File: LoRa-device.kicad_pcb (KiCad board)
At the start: 2 copper layers, 86.4 x 50.8 mm, 102 parts, among them J1 USB_C_Receptacle_USB2.0_14P, J2 Conn_01x02_Pin, J3 Conn_Coaxial, J4 Conn_01x14_Pin, J5 U.FL, J6 Conn_01x04_Pin, J7 Conn_01x11_Pin, Q1 AO3401A, Q2 S8050, Q3 AO3401A, SW1 SW_Nidec_CAS-120A1, U1 ESP32-S3, U2 W25Q128JVS, U3 TP4055, U4 AMS1117-3.3, U5 Ai-Thinker-Ra-01, U6 USBLC6-2P6, U7 L70-R, Y1 32.768 kHz, Y2 40MHz(10ppm)

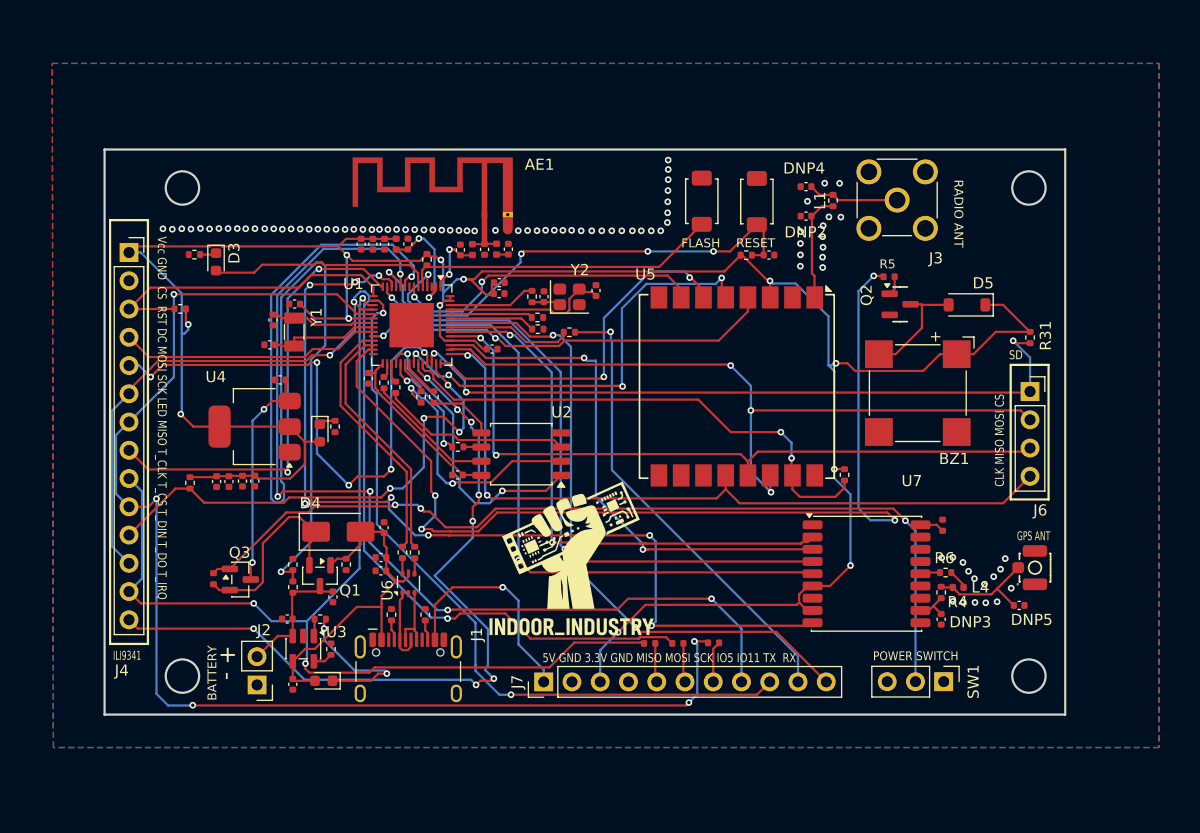
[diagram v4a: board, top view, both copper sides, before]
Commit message: Case work begun, 4 layers board
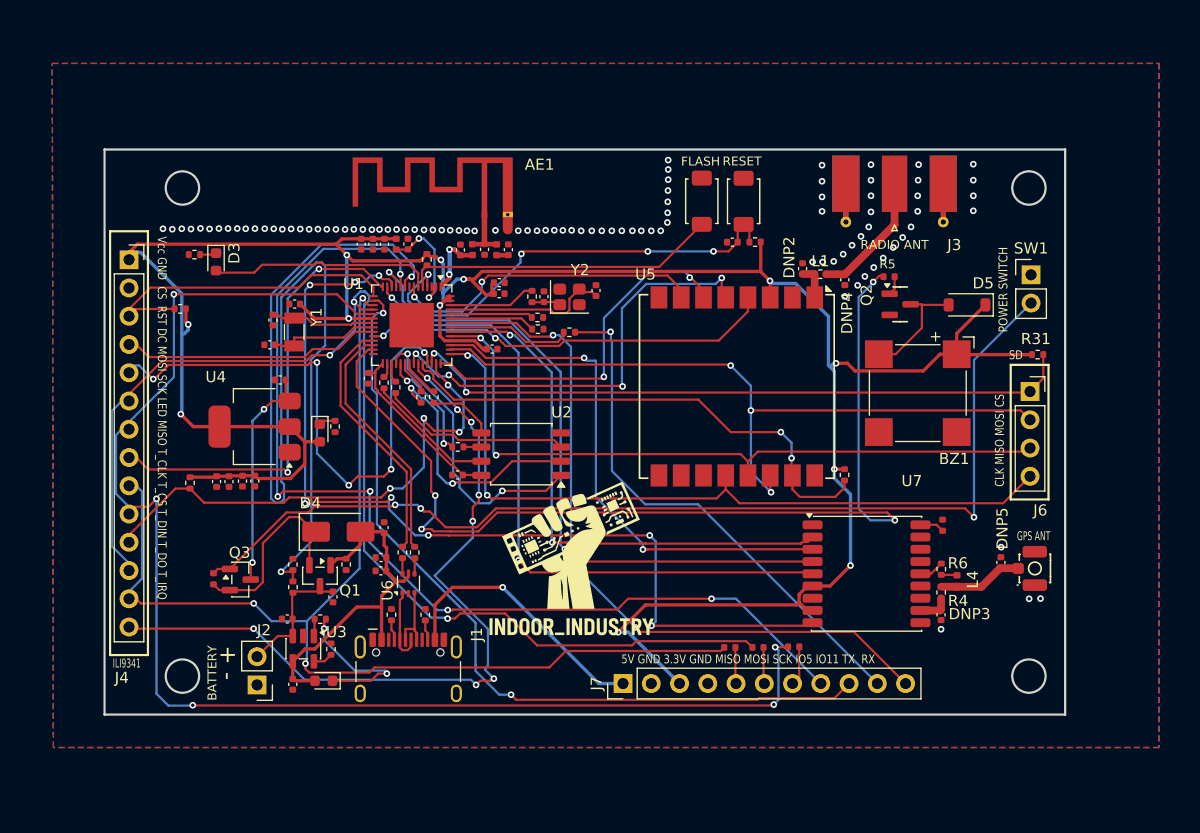
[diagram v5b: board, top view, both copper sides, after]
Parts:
- J3: footprint Connector_Coaxial:SMA_Molex_73251-2200_Horizontal -> Connector_Coaxial:SMA_Molex_73251-1153_EdgeMount_Horizontal
- SW1: footprint Connector_PinHeader_2.54mm:PinHeader_1x03_P2.54mm_Vertical -> Connector_PinHeader_2.54mm:PinHeader_1x02_P2.54mm_Vertical
- moved SW1 37.4 mm to (185.2, 85.1), turned to 0 degrees
- moved DNP4 9.07 mm to (168.4, 85.5), turned to -90 degrees
- moved R32 7.21 mm to (158.1, 118.6)
- moved R33 7.21 mm to (160.6, 118.6)
- moved R34 7.21 mm to (163.8, 118.5)
- moved J7 7.13 mm to (148.5, 121.8)
- moved L1 6.72 mm to (166.2, 85.0), turned to 0 degrees
- moved DNP2 4.73 mm to (164.7, 84.5), turned to 90 degrees
- moved DNP5 4.19 mm to (182.5, 111.0), turned to 90 degrees
- moved C15 3.49 mm to (158.3, 82.2), turned to 180 degrees
- moved R31 1.68 mm to (185.8, 92.3), turned to 0 degrees
- moved R22 1.42 mm to (160.4, 82.2), turned to 0 degrees
- moved RESET1 1.19 mm to (159.3, 78.5)
- moved J4 0.65 mm to (104.1, 83.8)
- moved L4 0.62 mm to (178.5, 112.6), turned to -90 degrees
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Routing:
- net Net-(Q3-G): track 81.6 -> 94.2 mm
- net IO11: track 66.3 -> 73.8 mm
- net RX: track 58.8 -> 66.0 mm
- net MOSIB: track 101.3 -> 108.3 mm
- net MISOB: track 96.7 -> 103.7 mm
- net SCKB: track 116.3 -> 123.2 mm
- net Net-(U5-ANT): track 9.73 -> 3.40 mm
- net TX: track 41.7 -> 47.5 mm
- net VDD_CPU: track 232.3 -> 238.0 mm
- net 5V: track 53.4 -> 57.8 mm
- net IO5: track 89.1 -> 93.5 mm
- net Net-(J3-In): track 8.21 -> 11.7 mm
- net IO35: track 63.4 -> 60.4 mm, vias 3 -> 2
- net EN: track 44.0 -> 41.2 mm
- net Net-(J5-In): track 10.3 -> 7.64 mm
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- added copper zone on In1.Cu, net GND
- added copper zone on In2.Cu, net GND
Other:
- copper layers 2 -> 4

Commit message: Further refinements
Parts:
- added TP1: TestPoint_2Pole, TestPoint:TestPoint_2Pads_Pitch2.54mm_Drill0.8mm, F.Cu at (144.1, 90.2)
- D4: footprint Diode_SMD:D_SMA -> LED_SMD:LED_0603_1608Metric
- D5: footprint Diode_SMD:D_SOD-123 -> LED_SMD:LED_0603_1608Metric
- J1: value USB_C_Receptacle_USB2.0_14P -> Connector, USB-TYPE-C-16P; footprint Connector_USB:USB_C_Receptacle_HCTL_HC-TYPE-C-16P-01A -> PCM_JLCPCB:TYPE-C-SMD_HX-TYPE-C-16PIN
- J7: value Conn_01x11_Pin -> Screw_Terminal_01x08; footprint Connector_PinHeader_2.54mm:PinHeader_1x11_P2.54mm_Vertical -> Connector_Phoenix_MC:PhoenixContact_MC_1,5_8-G-3.81_1x08_P3.81mm_Horizontal
- R3, R32, R33, R34, R5, R7: footprint PCM_JLCPCB:R_0402 -> Resistor_SMD:R_0402_1005Metric
- moved R28 6.32 mm to (129.2, 96.1), turned to -90 degrees
- moved C22 4.76 mm to (123.6, 111.1)
- moved R33 4.17 mm to (157.1, 116.4), turned to 0 degrees
- moved C6 4.07 mm to (123.7, 113.2), turned to -90 degrees
- moved J7 3.52 mm to (145.7, 119.7), turned to 0 degrees
- moved R24 3.14 mm to (140.8, 91.6)
- moved R32 2.75 mm to (159.8, 116.4)
- moved R34 2.65 mm to (162.3, 116.4)
- moved R13 2.49 mm to (109.7, 90.5)
- moved R18 2.47 mm to (129.8, 112.5)
- moved R2 2.47 mm to (128.7, 112.5)
- moved C16 2.38 mm to (124.8, 113.2), turned to -90 degrees
- moved U6 2.26 mm to (129.2, 115.1)
- moved C32 2.11 mm to (135.2, 104.5)
- moved J1 1.29 mm to (129.2, 120.4)
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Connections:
- J1 pad A8: (no net) -> unconnected-(J1-SBU1-PadA8)
- J1 pad B8: (no net) -> unconnected-(J1-SBU2-PadB8)
- J7 pad 2: GND -> VDD_CPU
- J7 pad 3: VDD_CPU -> GND
- J7 pad 4: GND -> Net-(J7-Pin_4)
- J7 pad 7: Net-(J7-Pin_7) -> IO5
- J7 pad 8: IO5 -> IO11
- R32 pad 2: MISOB -> MISOA
- R33 pad 1: Net-(J7-Pin_6) -> Net-(J7-Pin_4)
- R33 pad 2: MOSIB -> SCKA
- R34 pad 1: Net-(J7-Pin_7) -> Net-(J7-Pin_6)
- R34 pad 2: SCKB -> MOSIA
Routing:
- net SCKB: track 123.2 -> 40.1 mm, vias 5 -> 1
- net MOSIB: track 108.3 -> 43.3 mm, vias 3 -> 2
- net RX: track 66.0 -> 15.3 mm, vias 2 -> 0
- net IO4/BAT: track 92.5 -> 45.1 mm
- net MISOB: track 103.7 -> 57.0 mm, vias 3 -> 1
- net TX: track 47.5 -> 3.32 mm, vias 1 -> 0
- net IO47: track 70.3 -> 51.5 mm, vias 8 -> 3
- net SCKA: track 67.2 -> 82.1 mm, vias 2 -> 4
- net MISOA: track 64.0 -> 76.6 mm, vias 2 -> 4
- net MOSIA: track 65.7 -> 77.8 mm, vias 3 -> 4
- net IO21: track 89.9 -> 78.2 mm
- net IO34: track 49.2 -> 39.3 mm, vias 5 -> 3
- net 5V: track 57.8 -> 49.1 mm, vias 1 -> 0
- net Net-(U1-SPICLK): track 10.1 -> 2.80 mm, vias 2 -> 0
- net SPISCK: track 1.61 -> 8.24 mm
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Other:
- board text added: "5V 3.3V GND SCK MISO MOSI IO5 IO11"
- board text removed: "5V GND 3.3V GND MISO MOSI SCK IO5 IO11 TX RX"

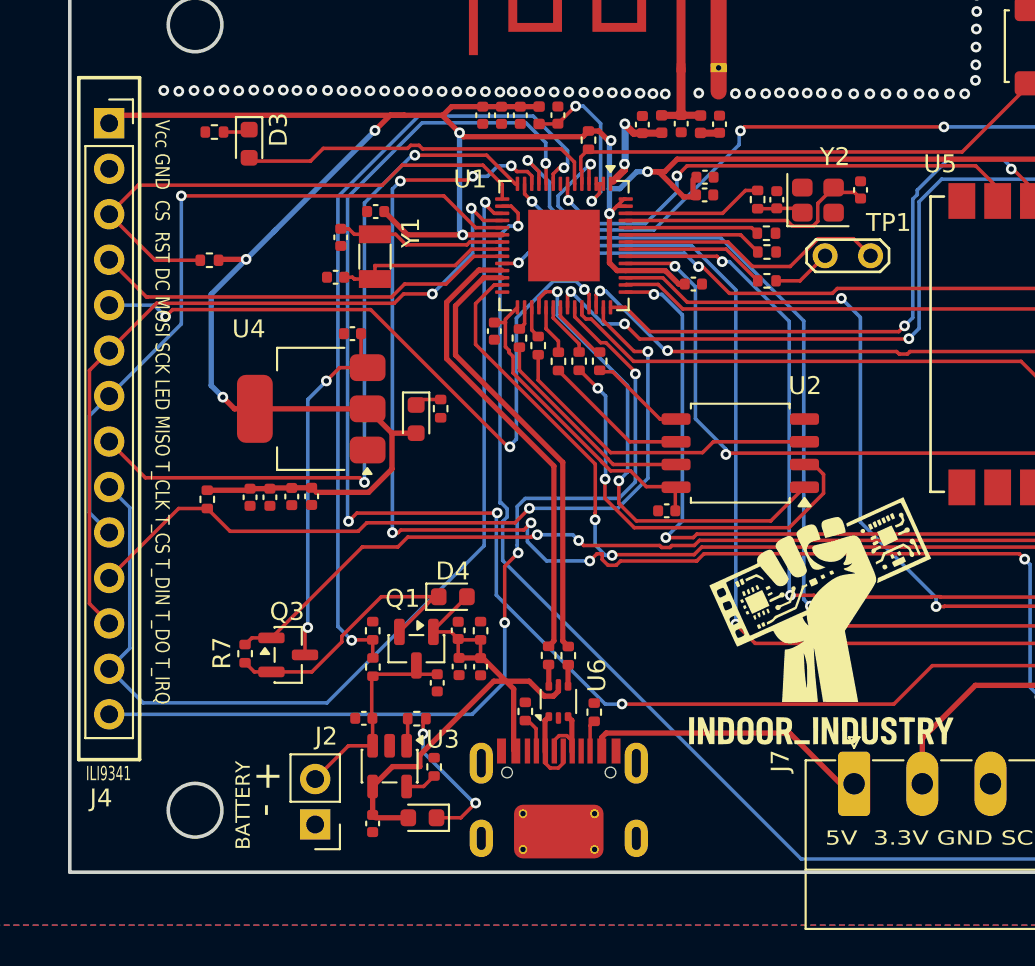
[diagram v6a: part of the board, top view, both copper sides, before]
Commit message: Power supply overhaul
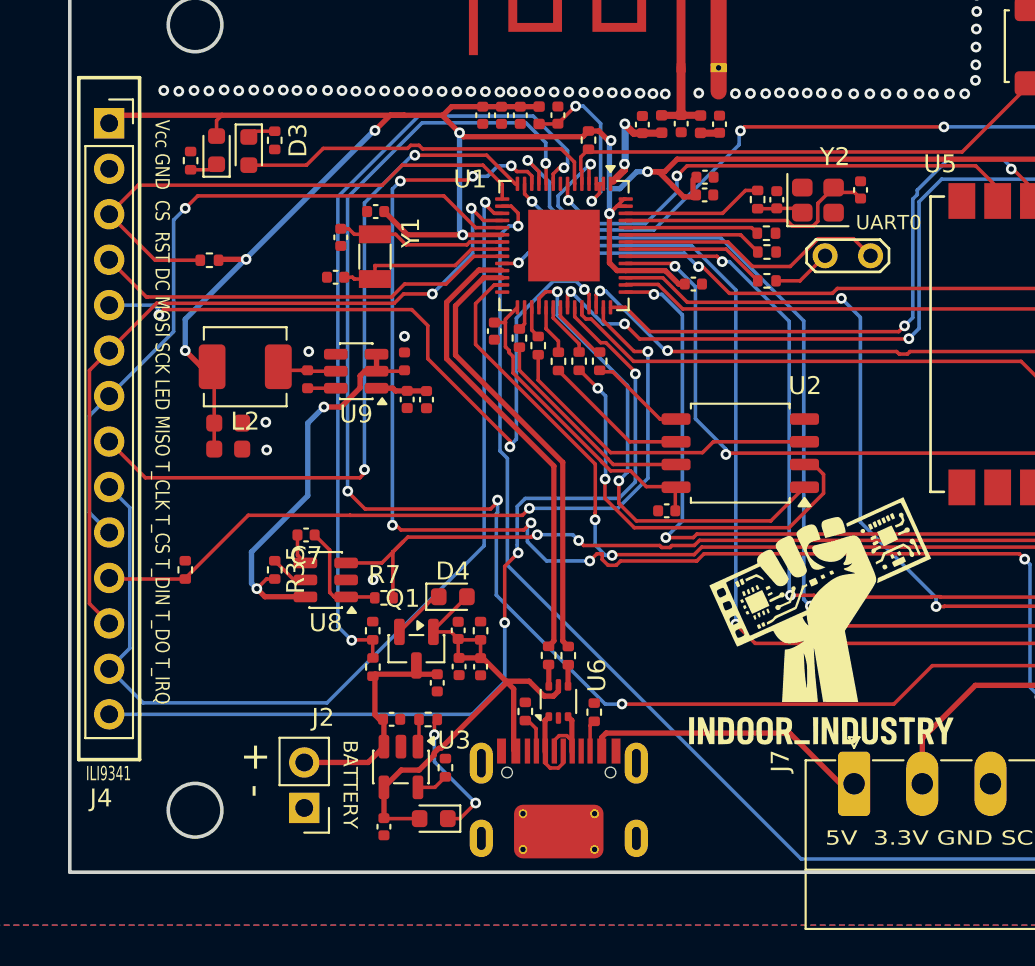
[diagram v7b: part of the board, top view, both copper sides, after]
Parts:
- removed C20: 10uF, Capacitor_SMD:C_0402_1005Metric
- removed C35: 0.1uF, Capacitor_SMD:C_0402_1005Metric
- removed Q3: AO3401A, Package_TO_SOT_SMD:SOT-23
- removed U4: AMS1117-3.3, Package_TO_SOT_SMD:SOT-223-3_TabPin2
- added C12: 22uF, PCM_JLCPCB:C_0603, F.Cu at (110.8, 99.5)
- added C21: 22uF, PCM_JLCPCB:C_0603, F.Cu at (110.8, 101.0)
- added C5: 10uF, PCM_JLCPCB:C_0402, F.Cu at (120.6, 96.1)
- added C9: 100nF, PCM_JLCPCB:C_0402, F.Cu at (115.2, 97.1)
- added L2: 4.7uH 3V, Inductor_SMD:L_Sunlord_MWSA0402S, F.Cu at (111.7, 96.4)
- added R35: DNP, Resistor_SMD:R_0402_1005Metric, F.Cu at (113.3, 107.8)
- added U8: TPS22917LDBV, Package_TO_SOT_SMD:SOT-23-6, F.Cu at (116.2, 108.3)
- added U9: AP63203WU, Package_TO_SOT_SMD:TSOT-23-6, F.Cu at (117.9, 96.7)
- C7: value 10uF -> DNP
- moved R16 19.7 mm to (108.7, 84.9), turned to 90 degrees
- moved D2 18.7 mm to (110.1, 84.3), turned to 90 degrees
- moved C7 11.5 mm to (115.1, 105.8)
- moved C3 10.3 mm to (120.8, 98.2)
- moved C17 8.39 mm to (121.8, 98.2)
- moved R7 8.36 mm to (119.5, 109.3), turned to 180 degrees
- moved R11 4.13 mm to (108.3, 107.8)
- moved R25 3.40 mm to (113.3, 83.8), turned to -90 degrees
- moved C2 1.56 mm to (119.9, 116.1), turned to 0 degrees
- moved J2 1.11 mm to (115.0, 121.0)
- moved C1 0.66 mm to (119.5, 122.1)
- moved D1 0.63 mm to (122.2, 121.6)
- moved R1 0.63 mm to (122.9, 118.8)
- moved R15 0.63 mm to (121.9, 116.1)
- moved U3 0.63 mm to (120.4, 118.8)
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- renumbered TP1 to UART0
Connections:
- C7 pad 1: VSYS_SW -> VSYS
- C7 pad 2: GND -> Net-(U8-CT)
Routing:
- net VDD_CPU: track 232.7 -> 216.3 mm
- net VSYS: track 16.0 -> 9.21 mm
- net Net-(SW1-B): track 93.1 -> 88.9 mm
- net Net-(U9-SW): track 0.00 -> 3.32 mm
- net VSYS_SW: track 20.5 -> 22.8 mm
- net Net-(U8-QOD): track 0.00 -> 2.16 mm
- net Net-(U8-CT): track 0.00 -> 1.75 mm
- net Net-(U9-BST): track 0.00 -> 1.58 mm
- net VBAT: track 12.0 -> 13.5 mm
- net IO34: track 39.3 -> 40.7 mm
- net IO36: track 44.5 -> 43.5 mm
- net Net-(D1-K): track 8.58 -> 7.82 mm
- net 5V: track 49.1 -> 48.4 mm
- net SCKB: track 40.1 -> 39.5 mm
- net IO9: track 41.1 -> 40.6 mm
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
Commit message: Added secure component
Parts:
- removed DNP3, DNP5: ~, Capacitor_SMD:C_0402_1005Metric
- removed J5: U.FL, PCM_JLCPCB:IPEX-SMD_BWIPX-1-001E
- removed L4: DNP, Inductor_SMD:L_0402_1005Metric
- removed R35: DNP, Resistor_SMD:R_0402_1005Metric
- removed R4, R6: 0R, Resistor_SMD:R_0402_1005Metric
- removed U7: L70-R, RF_GPS:Quectel_L70-R
- added C20: 10uF, PCM_JLCPCB:C_0402, F.Cu at (161.2, 113.7)
- added C23: 100nF, PCM_JLCPCB:C_0402, F.Cu at (162.2, 113.7)
- added C24: 33pF, PCM_JLCPCB:C_0402, F.Cu at (163.2, 113.7)
- added C27: 100pF, PCM_JLCPCB:C_0402, F.Cu at (179.7, 113.2)
- added C28: 100pF, PCM_JLCPCB:C_0402, F.Cu at (178.1, 110.5)
- added C29: 100nF, PCM_JLCPCB:C_0402, F.Cu at (177.1, 110.5)
- added C35: 1nF, PCM_JLCPCB:C_0402, F.Cu at (115.0, 105.8)
- added C36: 100nF, PCM_JLCPCB:C_0402, F.Cu at (161.2, 84.4)
- added DNP6: ~, Capacitor_SMD:C_0402_1005Metric, F.Cu at (177.1, 115.8)
- added DNP7: ~, Capacitor_SMD:C_0402_1005Metric, F.Cu at (178.2, 113.7)
- added J8: U.FL, PCM_JLCPCB:IPEX-SMD_BWIPX-1-001E, F.Cu at (184.8, 111.5)
- added L7: DNP, Inductor_SMD:L_0402_1005Metric, F.Cu at (179.6, 112.0)
- added R36: 0R, Resistor_SMD:R_0402_1005Metric, F.Cu at (177.5, 112.0)
- added U11: L76KB-A58, Lora-device:GPSM-SMD_18P-L10.1-W9.7-P1.10, F.Cu at (170.4, 112.2)
- added U4: ATECC608A-SSHDA, Package_SO:SOIC-8_3.9x4.9mm_P1.27mm, F.Cu at (121.5, 102.2)
- C7: value DNP -> 10uF; footprint Capacitor_SMD:C_0402_1005Metric -> PCM_JLCPCB:C_0402
- R3: value 0Ω -> 0R
- R8: value 10K -> 0Ω
- R9: value 10K -> 0R
- moved R3 63.9 mm to (113.3, 107.8), turned to -90 degrees
- moved C7 51.2 mm to (161.2, 83.5)
- moved R9 43.9 mm to (177.1, 113.7), turned to 90 degrees
- moved R8 40.6 mm to (177.1, 108.3), turned to -90 degrees
- moved R24 1.69 mm to (140.3, 90.0)
- moved G*** 0.87 mm to (144.4, 111.3)
- renumbered UART0 to TP1
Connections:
- C7 pad 1: VSYS -> VDD_CPU
- C7 pad 2: Net-(U8-CT) -> GND
- J4 pad 14: IO47 -> unconnected-(J4-Pin_14-Pad14)
- R3 pad 1: Net-(R3-Pad1) -> Net-(U8-QOD)
- R3 pad 2: GND -> VSYS_SW
- R8 pad 1: IO45 -> Net-(U11-SET)
- R9 pad 1: IO46 -> Net-(U11-RF_IN)
- R9 pad 2: GND -> Net-(C27-Pad1)
- U1 pad 51: IO45 -> unconnected-(U1-GPIO45-Pad51)
- U1 pad 52: IO46 -> unconnected-(U1-GPIO46-Pad52)
- U5 pad 5: IO48 -> IO2
- U5 pad 6: IO37 -> IO47
- U5 pad 7: IO2 -> unconnected-(U5-DIO2-Pad7)
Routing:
- net VDD_CPU: track 216.3 -> 245.6 mm, vias 12 -> 14
- net IO2: track 28.6 -> 0.51 mm, vias 2 -> 0
- net IO48: track 39.6 -> 21.0 mm, vias 4 -> 2
- net IO47: track 51.5 -> 37.5 mm, vias 3 -> 2
- net IO37: track 33.6 -> 24.2 mm
- net IO45: track 7.78 -> 0.00 mm
- net Net-(J5-In): track 7.64 -> 0.00 mm
- net IO46: track 7.48 -> 0.00 mm
- net Net-(J8-In): track 0.00 -> 6.34 mm
- net Net-(C28-Pad1): track 0.00 -> 4.54 mm
- net Net-(U7-RF_IN): track 2.89 -> 0.00 mm
- net Net-(U11-RF_IN): track 0.00 -> 2.89 mm
- net IO11: track 77.3 -> 80.0 mm
- net IO5: track 96.7 -> 99.2 mm
- net Net-(U7-VCC_RF): track 2.41 -> 0.00 mm
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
